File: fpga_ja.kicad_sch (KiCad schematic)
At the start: 19 parts, among them J1 Conn_02x07_Odd_Even, SW2 SW_Push, SW3 SW_DIP_x04, U16 Kria K24 SoM

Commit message: Imon Schematic and DRC checking changes -Added current monitor ADC for Imon -Fixed unconnected nets -Added shorting resistor between both output power on signals from Kria SoM
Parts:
- added C26: 2.2u, Capacitor_SMD:C_0402_1005Metric, symbol Device:C_Small
- added C30, C32: 100n, Capacitor_SMD:C_0402_1005Metric, symbol Device:C_Small
- added R100, R99: 4.7k, Resistor_SMD:R_0402_1005Metric, symbol Device:R_Small
- added R101: 0, Resistor_SMD:R_0402_1005Metric, symbol Device:R_Small
- added U31: MCP3221, Package_TO_SOT_SMD:SOT-23-5, symbol Analog_ADC:MCP3221
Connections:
- net +3V3: now also C26.1, C30.2, C32.2, R100.2, R99.2, U31.1 (V_{DD})
- net GND: now also C26.2, C30.1, C32.1, U31.2 (V_{SS})
- net PL_SUPPLY_START: now also R101.1
- net PS_SUPPLY_START: now also R101.2
- net i2c_33_scl: now reaches U16.JA_C22 (HDA_18)
- net i2c_33_scl: now also R99.1, U31.5 (SCL)
- net i2c_33_sda: now reaches U16.JA_C23 (HDA_19)
- net i2c_33_sda: now also R100.1, U31.4 (SDA)
- new net Imon: U31.3 (A_{IN})

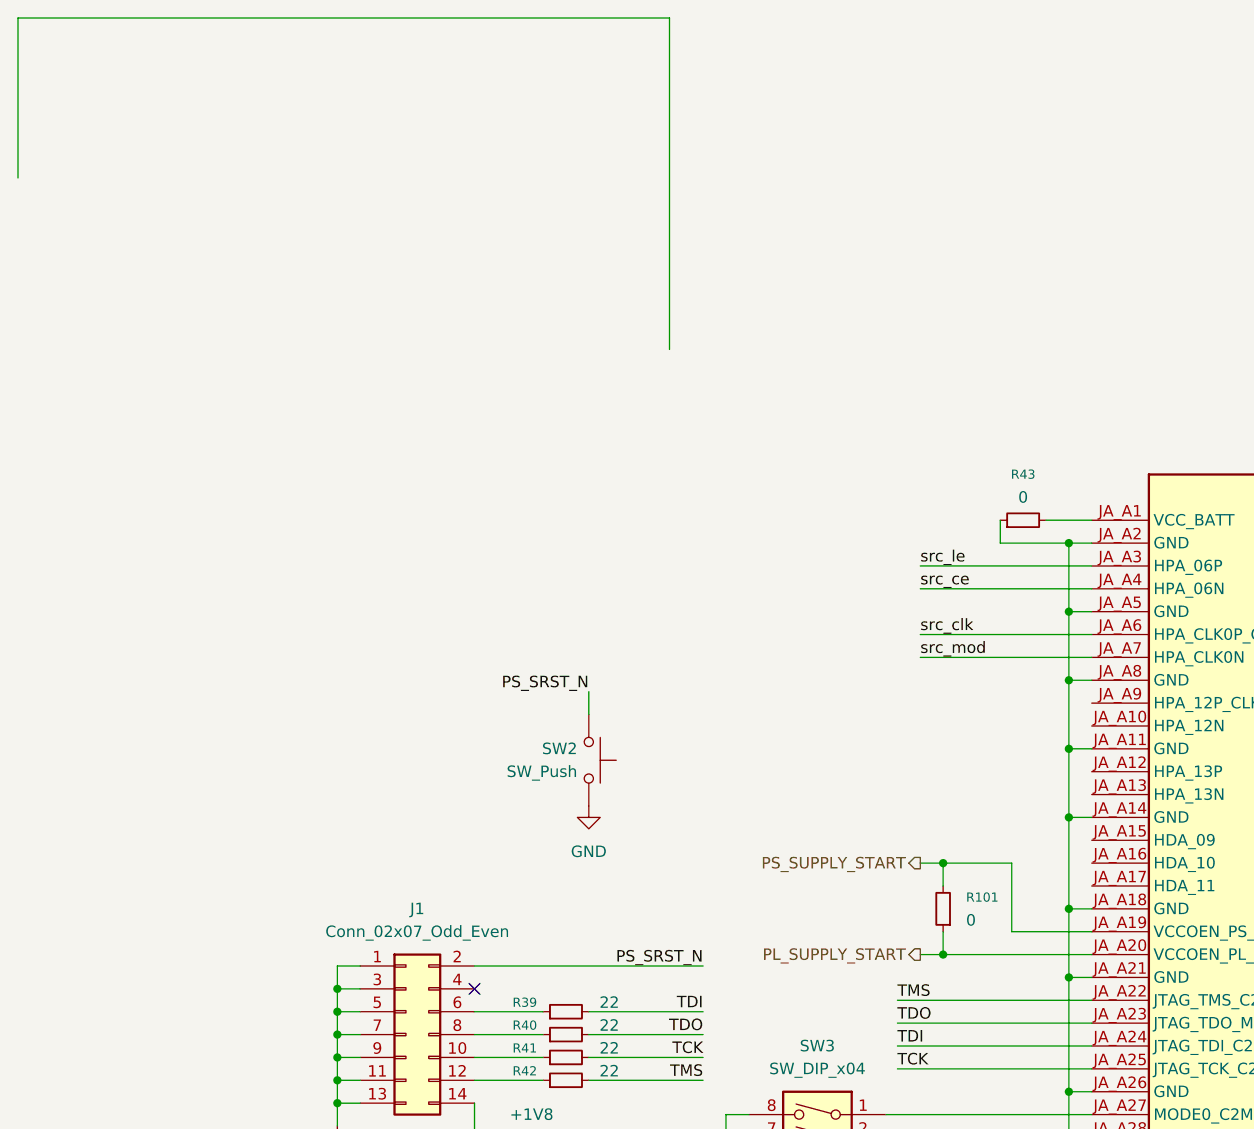
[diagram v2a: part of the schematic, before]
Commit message: Schematic and layout updates:
-Removed some extraneous wires on schematic sheets. May be some more.
-Length matched RGMII and ULPI. Maybe need to look at TFT.
-Updated some digikey part numbers.
-Added some extra file nonesense to .gitignore
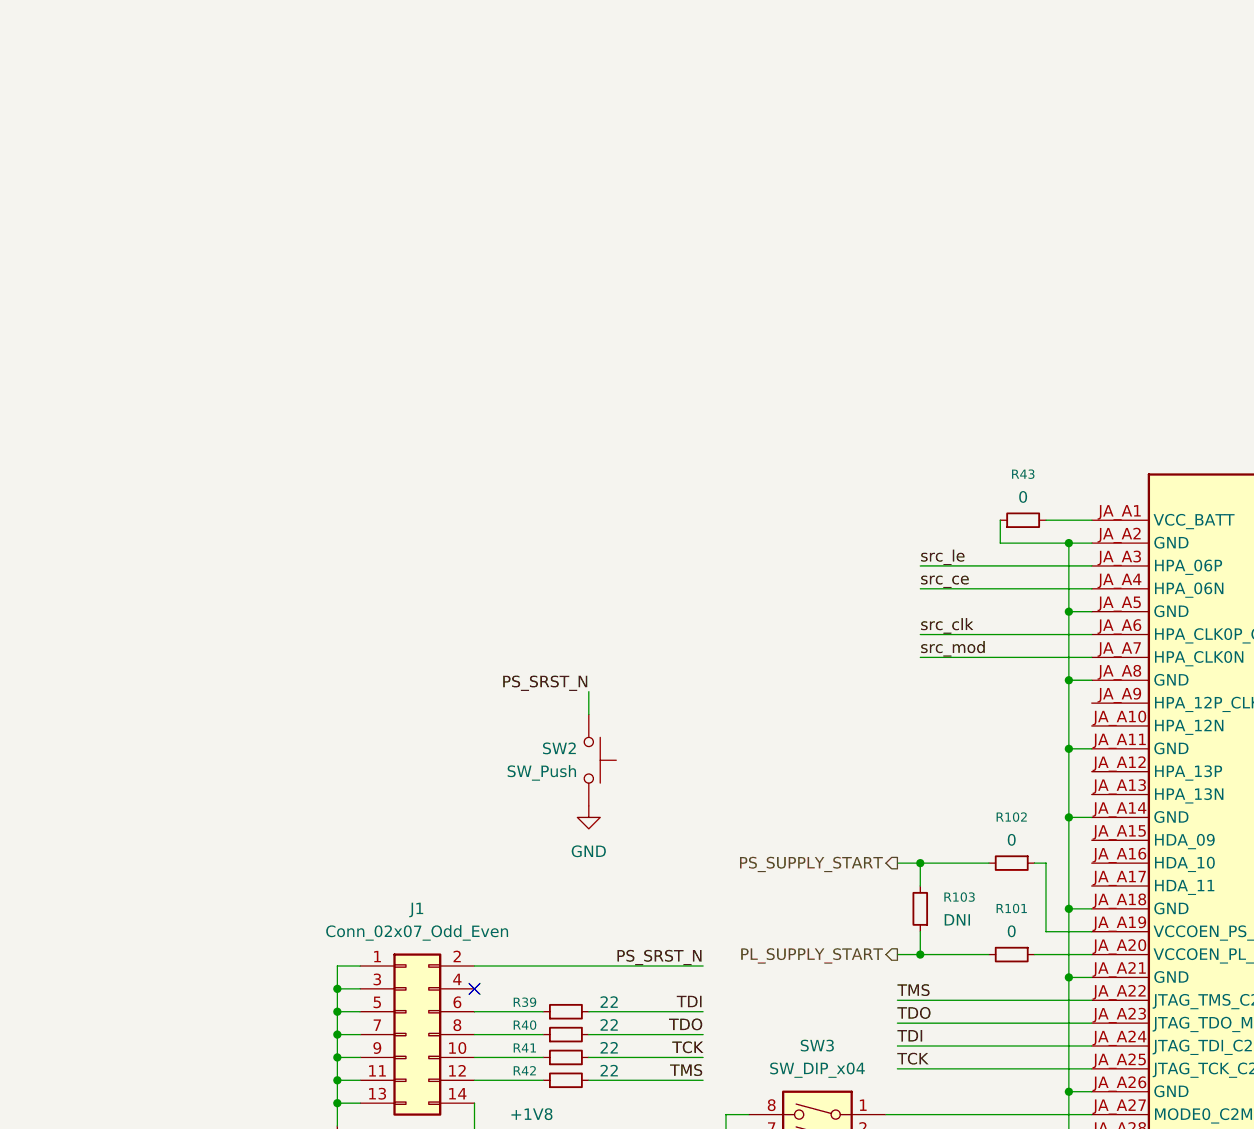
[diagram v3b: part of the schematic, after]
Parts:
- added R102: 0, Resistor_SMD:R_0402_1005Metric, symbol Device:R_Small
- added R103: DNI, Resistor_SMD:R_0402_1005Metric, symbol Device:R_Small
- C30, C32: Digikey PN (none) -> 1276-1043-1-ND
- R100, R99: Digikey PN (none) -> 311-4.7KJRCT-ND
- R101, R43: Digikey PN (none) -> 311-0.0JRCT-ND
- R39, R40, R41, R42, R44, R45, R46, R47, R48, R49, R50: Digikey PN (none) -> 541-22.0LCT-ND
- R95: Digikey PN (none) -> 311-470LRCT-ND
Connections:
- net PL_SUPPLY_START: now also R101.2, R103.1; no longer R101.1, U16.JA_A20 (VCCOEN_PL_M2C)
- net PS_SUPPLY_START: now also R102.2, R103.2; no longer R101.2, U16.JA_A19 (VCCOEN_PS_M2C)
- new net: R101.1, U16.JA_A20 (VCCOEN_PL_M2C)
- new net: R102.1, U16.JA_A19 (VCCOEN_PS_M2C)
